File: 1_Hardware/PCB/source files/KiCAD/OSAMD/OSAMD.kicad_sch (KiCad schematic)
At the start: 15 parts, among them J1 DHT11-Socket, J2 MQ-135 Conn, J3 LCD Conn, J4 Socket_Arduino16_30, J5 Socket_Arduino01_15, J6 Barrel_Jack, SW1 SW_Pushbutton

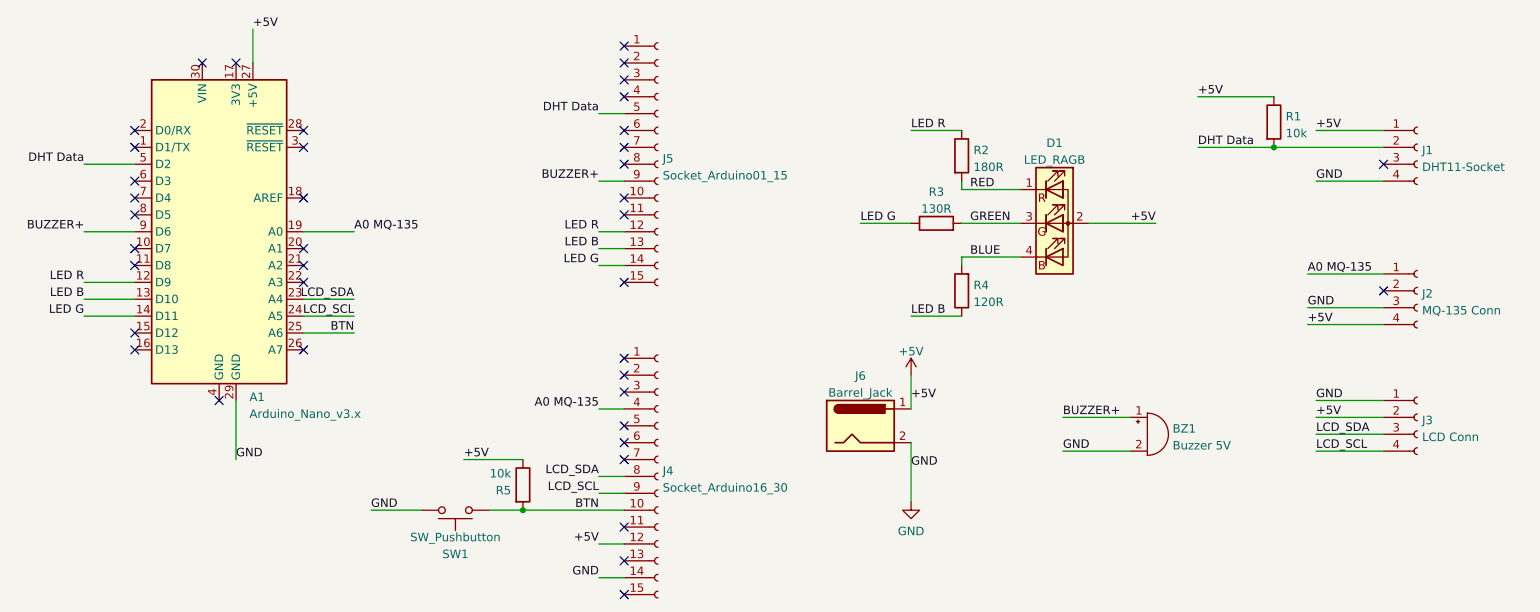
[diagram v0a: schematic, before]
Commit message: switched button and buzzer pin
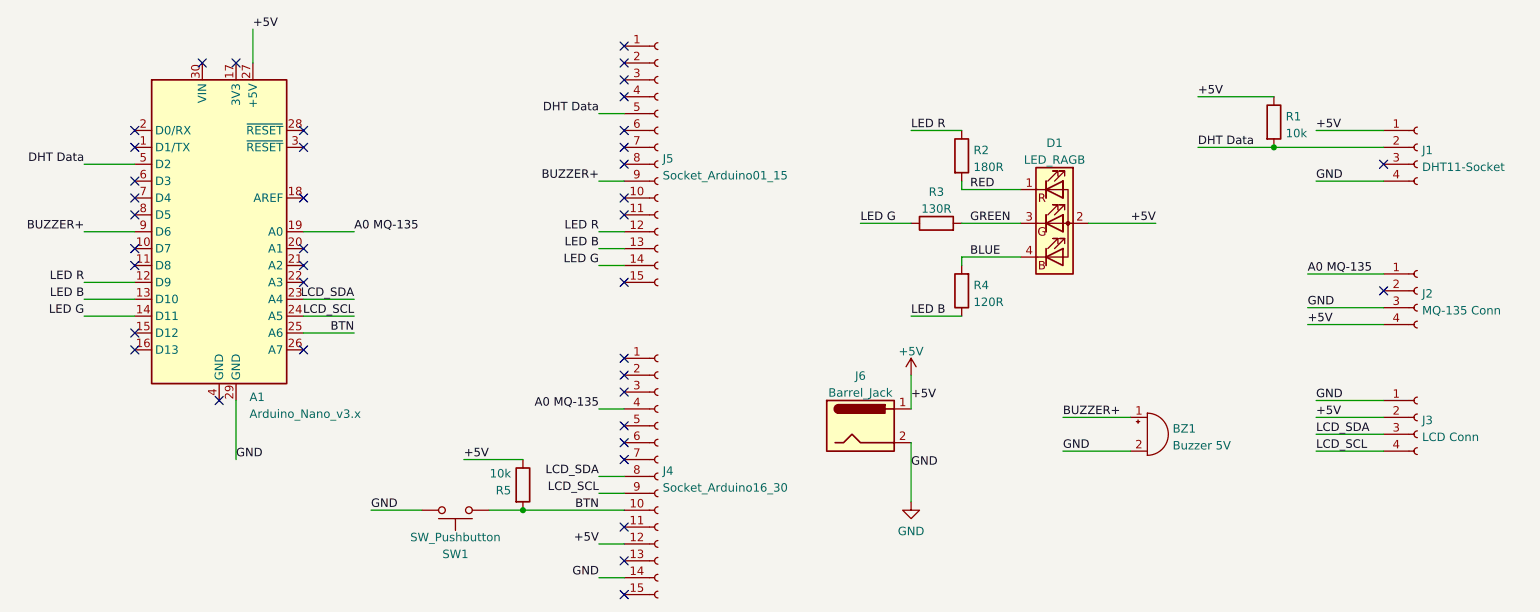
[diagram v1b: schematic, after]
